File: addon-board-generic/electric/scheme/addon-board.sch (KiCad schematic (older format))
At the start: 59 parts

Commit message: Placing components...
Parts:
- removed K? (x2): CONN_3, symbol CONN_3
- removed P?: CONN_8, symbol CONN_8
- added P10: CONN_6, symbol CONN_6
- gave numbers to parts that had none: 56
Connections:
- net labels removed: adc6, adc7, adc8, servo7, servo8
- wire segments 305 -> 296

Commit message: Added shift registers to increase IO pins number.
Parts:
- removed P10: CONN_6, symbol CONN_6
- added K7, K8: CONN_3, symbol CONN_3
- added P10: CONN_8, symbol CONN_8
- added U4, U5: 74HC595_MY, symbol 74HC595_MY
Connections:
- net labels added: adc6, adc7, ds, mr, oe, servo7, servo8, shcp, stcp
- wire segments 296 -> 344
- no-connect marks 7 -> 15

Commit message: Started routing.
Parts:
- added C10, C9: 18p, symbol C
- added C8: 10u, ~, symbol C
- added R20: 50, symbol R
- added X1: 8MHz, symbol CRYSTAL
- C7: value 10u -> 100n
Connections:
- wire segments 344 -> 351
- no-connect marks 15 -> 14
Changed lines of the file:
@@
 Sheet 1 1
 Title ""
-Date "2 sep 2013"
+Date "6 sep 2013"
 Rev ""
 Comp ""
@@
 P 24650 2450
 F 0 "C7" H 24650 2550 40  0000 L CNN
-F 1 "10u" H 24656 2365 40  0000 L CNN
+F 1 "100n" H 24656 2365 40  0000 L CNN
 F 2 "~" H 24688 2300 30  0000 C CNN
 F 3 "~" H 24650 2450 60  0000 C CNN
@@
 	1    0    0    -1
 $EndComp
-Text Label 5200 4850 0    60   ~ 0
+Text Label 5200 6450 0    60   ~ 0
 wakeup
 $Comp
@@
 	2050 8600 2500 8600
 Wire Wire Line
-	5850 4850 5150 4850
-Wire Wire Line
-	5850 5550 5150 5550
-Wire Wire Line
 	29600 21800 30000 21800
 Connection ~ 29700 20700
@@
 	24850 2450 25050 2450
 Wire Wire Line
-	25050 2450 25050 2000
+	25050 2000 25050 2650
 Connection ~ 25050 2000
 Wire Wire Line
@@
 ds
 NoConn ~ 5150 7150
-NoConn ~ 5150 6450
 Text Label 10800 7500 0    60   ~ 0
 servo7
@@
 adc7
 NoConn ~ 11300 2850
-NoConn ~ 5150 5550
+NoConn ~ 5450 5150
 NoConn ~ 21200 11200
 NoConn ~ 21200 11400
@@
 Wire Wire Line
 	26400 6400 26400 6500
+$Comp
+L C C8
+U 1 1 522A3633
+P 25050 2850
+F 0 "C8" H 25050 2950 40  0000 L CNN
+F 1 "10u" H 25056 2765 40  0000 L CNN
+F 2 "~" H 25088 2700 30  0000 C CNN
+F 3 "~" H 25050 2850 60  0000 C CNN
+	1    25050 2850
+	-1   0    0    1
+$EndComp
+Connection ~ 25050 2450
+Wire Wire Line
+	25050 3050 25050 3350
+$Comp
+L GND #PWR063
+U 1 1 522A3941
+P 25050 3350
+F 0 "#PWR063" H 25050 3350 30  0001 C CNN
+F 1 "GND" H 25050 3280 30  0001 C CNN
+F 2 "" H 25050 3350 60  0000 C CNN
+F 3 "" H 25050 3350 60  0000 C CNN
+	1    25050 3350
+	1    0    0    -1
+$EndComp
+$Comp
+L R R20
+U 1 1 522A4B5F
+P 5450 5550
+F 0 "R20" V 5530 5550 50  0000 C CNN
+F 1 "50" V 5450 5550 50  0000 C CNN
+F 2 "" H 5450 5550 60  0001 C CNN
+F 3 "" H 5450 5550 60  0001 C CNN
+	1    5450 5550
+	0    -1   -1   0
+$EndComp
+$Comp
+L GND #PWR064
+U 1 1 522A4B65
+P 4350 5700
+F 0 "#PWR064" H 4350 5700 30  0001 C CNN
+F 1 "GND" H 4350 5630 30  0001 C CNN
+F 2 "" H 4350 5700 60  0001 C CNN
+F 3 "" H 4350 5700 60  0001 C CNN
+	1    4350 5700
+	1    0    0    -1
+$EndComp
+$Comp
+L CRYSTAL X1
+U 1 1 522A4B6B
+P 5050 5200
+F 0 "X1" H 5050 5350 60  0000 C CNN
+F 1 "8MHz" H 5050 5050 60  0000 C CNN
+F 2 "" H 5050 5200 60  0001 C CNN
+F 3 "" H 5050 5200 60  0001 C CNN
+	1    5050 5200
+	0    -1   -1   0
+$EndComp
+$Comp
+L C C10
+U 1 1 522A4B71
+P 4650 5550
+F 0 "C10" H 4700 5650 50  0000 L CNN
+F 1 "18p" H 4700 5450 50  0000 L CNN
+F 2 "" H 4650 5550 60  0001 C CNN
+F 3 "" H 4650 5550 60  0001 C CNN
+	1    4650 5550
+	0    -1   -1   0
+$EndComp
+$Comp
+L C C9
+U 1 1 522A4B77
+P 4650 4850
+F 0 "C9" H 4700 4950 50  0000 L CNN
+F 1 "18p" H 4700 4750 50  0000 L CNN
+F 2 "" H 4650 4850 60  0001 C CNN
+F 3 "" H 4650 4850 60  0001 C CNN
+	1    4650 4850
+	0    -1   -1   0
+$EndComp
+Connection ~ 5050 5550
+Wire Wire Line
+	5200 5550 4850 5550
+Connection ~ 4350 5550
+Wire Wire Line
+	4350 5700 4350 4850
+Connection ~ 5050 4850
+Wire Wire Line
+	5050 4900 5050 4850
+Wire Wire Line
+	4850 4850 5850 4850
+Wire Wire Line
+	5050 5550 5050 5500
+Wire Wire Line
+	4350 4850 4450 4850
+Wire Wire Line
+	4350 5550 4450 5550
+Wire Wire Line
+	5700 5550 5850 5550
 $EndSCHEMATC

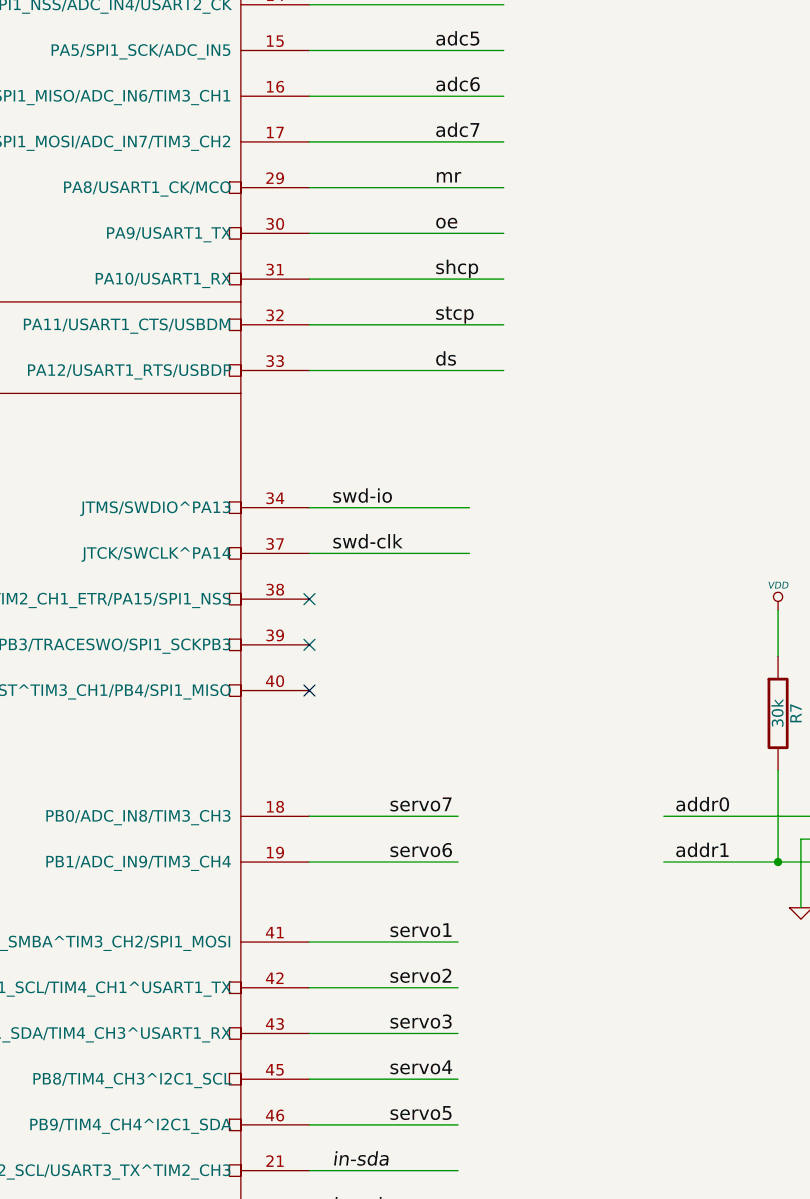
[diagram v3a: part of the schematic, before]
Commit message: Finished routing. Holes for supports and cross board socket matches should be checked!
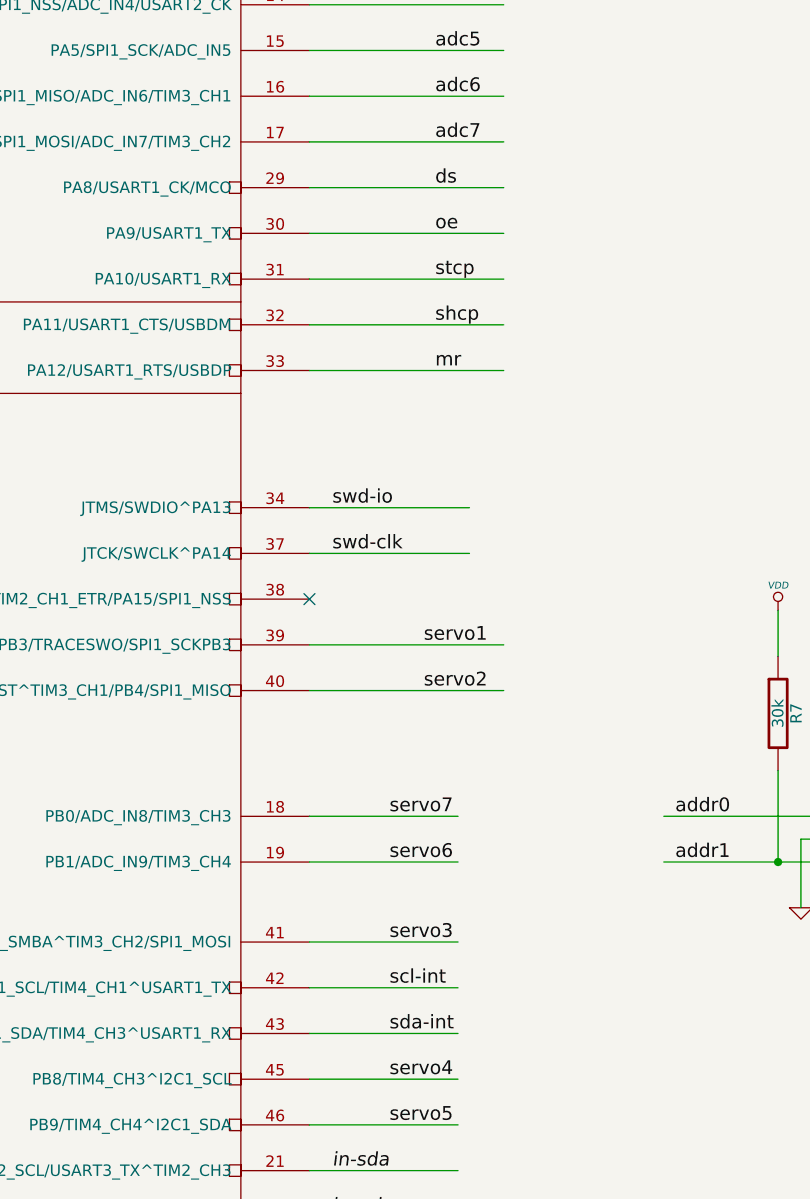
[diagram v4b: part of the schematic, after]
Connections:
- wire segments 351 -> 353
- no-connect marks 14 -> 12
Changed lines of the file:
@@
 Sheet 1 1
 Title ""
-Date "6 sep 2013"
+Date "7 sep 2013"
 Rev ""
 Comp ""
@@
 	0    1    1    0
 $EndComp
-NoConn ~ 10450 6950
-NoConn ~ 10450 6750
 $Comp
 L GND #PWR019
@@
 Text Label 21750 2800 0    60   ~ 0
 servo-en
+Text Label 10950 6750 0    60   ~ 0
+servo1
+Text Label 10950 6950 0    60   ~ 0
+servo2
 Text Label 10800 8050 0    60   ~ 0
-servo1
-Text Label 10800 8250 0    60   ~ 0
-servo2
-Text Label 10800 8450 0    60   ~ 0
 servo3
 Text Label 10800 8650 0    60   ~ 0
@@
 Text Label 20950 11000 0    60   ~ 0
 servo-en
-Text Label 11000 4750 0    60   ~ 0
+Text Label 11000 5550 0    60   ~ 0
 mr
 Text Label 11000 4950 0    60   ~ 0
 oe
+Text Label 11000 5350 0    60   ~ 0
+shcp
 Text Label 11000 5150 0    60   ~ 0
-shcp
-Text Label 11000 5350 0    60   ~ 0
 stcp
 Text Label 15800 11600 0    60   ~ 0
 ds
-Text Label 11000 5550 0    60   ~ 0
+Text Label 11000 4750 0    60   ~ 0
 ds
 NoConn ~ 5150 7150
@@
 Wire Wire Line
 	5700 5550 5850 5550
+Text Label 10800 8450 0    60   ~ 0
+sda-int
+Text Label 10800 8250 0    60   ~ 0
+scl-int
+Wire Wire Line
+	10450 6750 11300 6750
+Wire Wire Line
+	10450 6950 11300 6950
 $EndSCHEMATC

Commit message: Raplaced power mosfets with sot23 transistors because of their max current and very low resistance.
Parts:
- Q2, Q5, Q6: value MOS_P -> IRLML2244
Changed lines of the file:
@@
 Sheet 1 1
 Title ""
-Date "7 sep 2013"
+Date "10 sep 2013"
 Rev ""
 Comp ""
@@
 P 27900 17600
 F 0 "Q5" H 27900 17790 60  0000 R CNN
-F 1 "MOS_P" H 27900 17420 60  0000 R CNN
+F 1 "IRLML2244" H 27900 17420 60  0000 R CNN
 F 2 "" H 27900 17600 60  0001 C CNN
 F 3 "" H 27900 17600 60  0001 C CNN
@@
 P 27900 20300
 F 0 "Q6" H 27900 20490 60  0000 R CNN
-F 1 "MOS_P" H 27900 20120 60  0000 R CNN
+F 1 "IRLML2244" H 27900 20120 60  0000 R CNN
 F 2 "" H 27900 20300 60  0001 C CNN
 F 3 "" H 27900 20300 60  0001 C CNN
@@
 P 24100 2100
 F 0 "Q2" H 24100 2290 60  0000 R CNN
-F 1 "MOS_P" H 24100 1920 60  0000 R CNN
+F 1 "IRLML2244" H 24100 1920 60  0000 R CNN
 F 2 "~" H 24100 2100 60  0000 C CNN
 F 3 "~" H 24100 2100 60  0000 C CNN
